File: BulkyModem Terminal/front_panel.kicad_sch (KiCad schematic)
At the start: 24 parts, among them J3 Module_Panel, U5 74HCT04

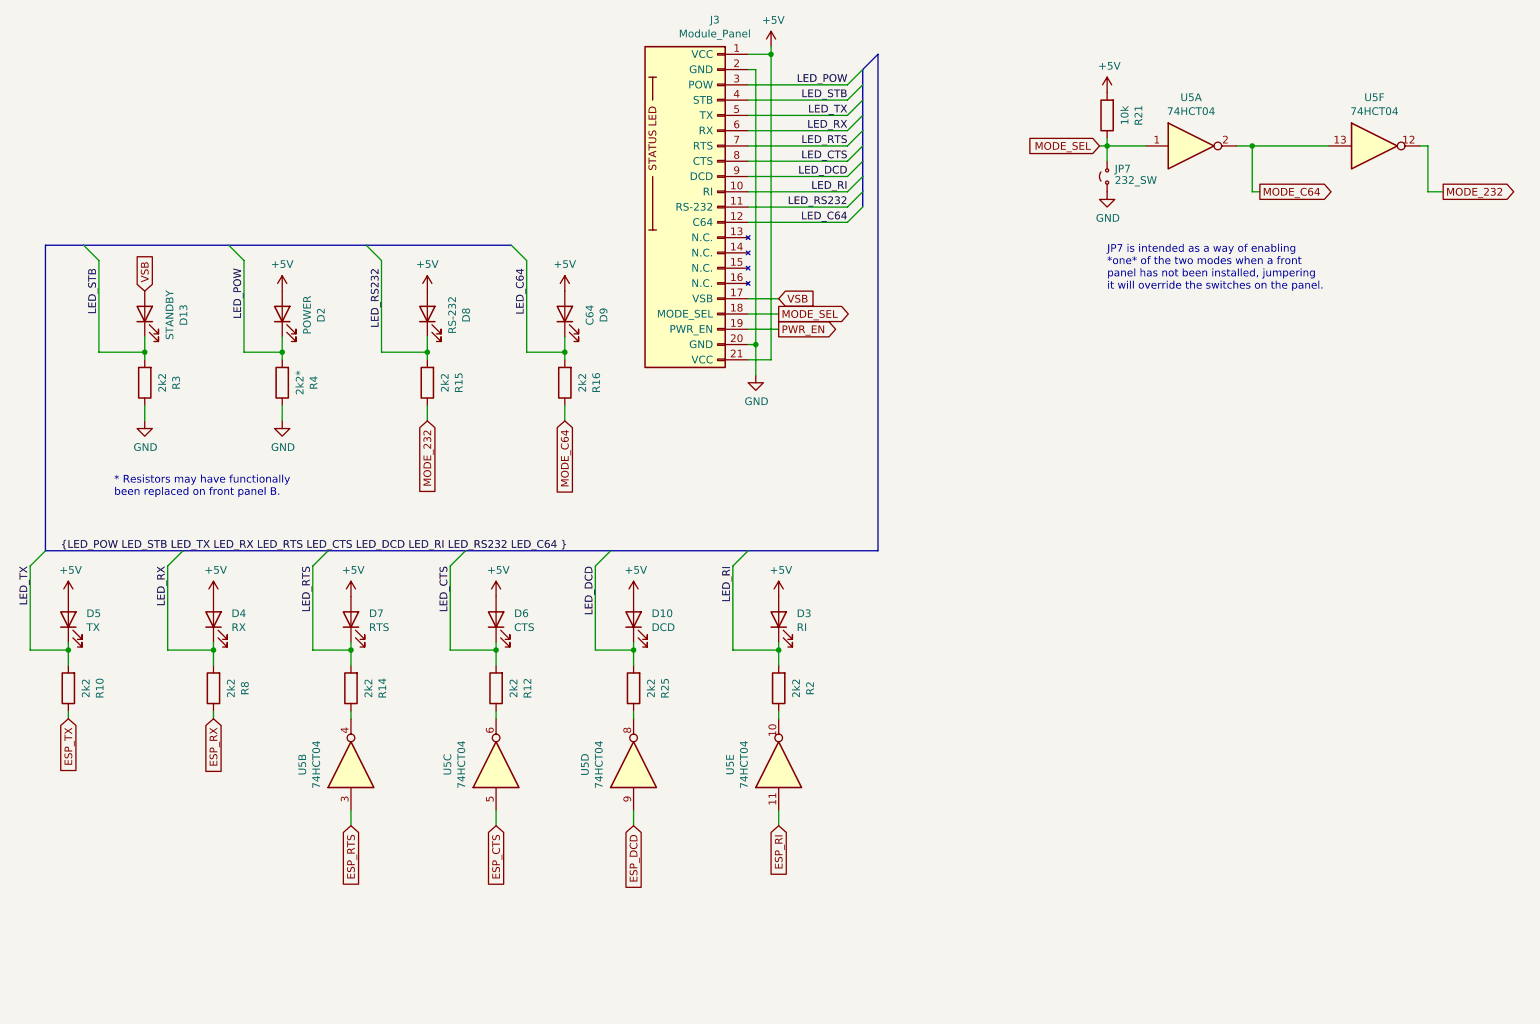
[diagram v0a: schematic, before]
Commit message: Terminal schematic (first draft)
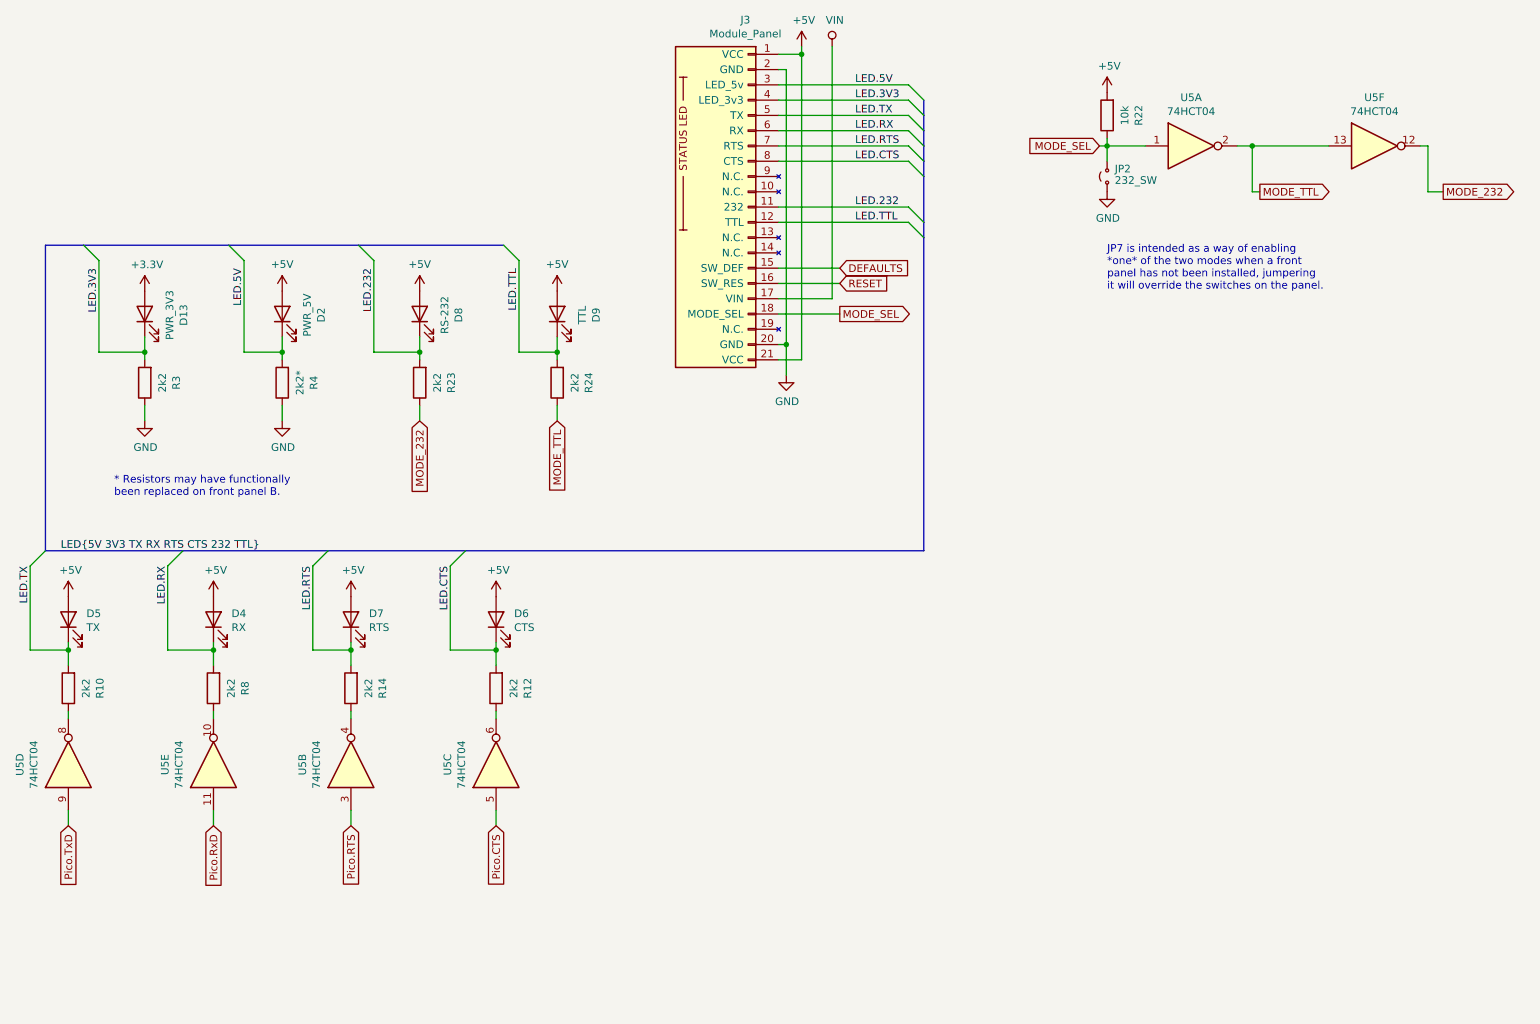
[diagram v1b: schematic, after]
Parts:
- removed D10: DCD, LED_THT:LED_D3.0mm, symbol Device:LED
- removed D3: RI, LED_THT:LED_D3.0mm, symbol Device:LED
- removed JP7: 232_SW, Connector_PinHeader_2.54mm:PinHeader_1x02_P2.54mm_Vertical, symbol Jumper:Jumper_2_Small_Open
- removed R15, R16, R2, R25: 2k2, resistor:R_Axial_DIN0207_L6.3mm_D2.5mm_P10.16mm_Horizontal, symbol Device:R
- removed R21: 10k, resistor:R_Axial_DIN0207_L6.3mm_D2.5mm_P10.16mm_Horizontal, symbol Device:R
- added JP2: 232_SW, Connector_PinHeader_2.54mm:PinHeader_1x02_P2.54mm_Vertical, symbol Jumper:Jumper_2_Small_Open
- added R22: 10k, resistor:R_Axial_DIN0207_L6.3mm_D2.5mm_P10.16mm_Horizontal, symbol Device:R
- added R23, R24: 2k2, resistor:R_Axial_DIN0207_L6.3mm_D2.5mm_P10.16mm_Horizontal, symbol Device:R
- D13: value STANDBY -> PWR_3V3
- D2: value POWER -> PWR_5V
- D9: value C64 -> TTL
- J3: symbol BulkyModem:Module_Panel -> BulkyModem:Terminal_Panel
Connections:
- net ESP_RX is gone; now on an unnamed net: R8.1
- net ESP_TX is gone; now on an unnamed net: R10.1
- net +5V: now also R22.2
- net GND: now also JP2.1 (A)
- net MODE_232: now also R23.1
- net MODE_SEL: now also JP2.2 (B), R22.1
- net DEFAULTS: now reaches J3.15 (SW_DEF)
- net RESET: now reaches J3.16 (SW_RES)
- net ESP_CTS renamed Pico.CTS
- net ESP_DCD renamed Pico.TxD
- net ESP_RI renamed Pico.RxD
- net ESP_RTS renamed Pico.RTS
- net LED_C64 renamed LED.TTL
- net LED.TTL: now also R24.2
- net LED_CTS renamed LED.CTS
- net LED_DCD: no longer names the net of J3.9 (N.C.)
- net LED_POW renamed LED.5V
- net LED_RI: no longer names the net of J3.10 (N.C.)
- net LED_RS232 renamed LED.232
- net LED.232: now also R23.2
- net LED_RTS renamed LED.RTS
- net LED_RX renamed LED.RX
- net LED_STB renamed LED.3V3
- net LED_TX renamed LED.TX
- net MODE_C64 renamed MODE_TTL
- net MODE_TTL: now also R24.1
- net PWR_EN: no longer names the net of J3.19 (N.C.)
- net VSB renamed +3.3V
- net +3.3V: no longer J3.17 (VSB)
- new net VIN: J3.17 (VIN)

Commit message: Part of a layout
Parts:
- removed D13: PWR_3V3, LED_THT:LED_D3.0mm, symbol Device:LED
- removed D2: PWR_5V, LED_THT:LED_D3.0mm, symbol Device:LED
- removed R3: 2k2, resistor:R_Axial_DIN0207_L6.3mm_D2.5mm_P10.16mm_Horizontal, symbol Device:R
- J3: footprint BulkyModem:Module_Panel -> BulkyModem:Terminal_Panel
- R4: value 2k2* -> 2k2
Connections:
- net LED.232: now also J3.9 (EN_232); no longer J3.11 (232)
- net LED.TTL: now also J3.10 (EN_TTL); no longer J3.12 (TTL)
- net LED.3V3: no longer names the net of J3.4 (N.C.)
- net LED.5V renamed LED.POW
- no-connect marks 0 -> 5
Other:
- note removed: "* Resistors may have functionally been replaced on front panel B."
- moved on the sheet: R4

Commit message: Added remaining tracks
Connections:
- no-connect marks 5 -> 6
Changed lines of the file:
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@@
+	)
+	(no_connect
+		(at 158.75 74.93)
 	)
 	(no_connect
@@
 		)
 	)
-	(label "LED{5V 3V3 TX RX RTS CTS 232 TTL}"
+	(label "LED{POW TX RX RTS CTS 232 TTL}"
 		(at 39.37 111.76 0)
 		(fields_autoplaced yes)

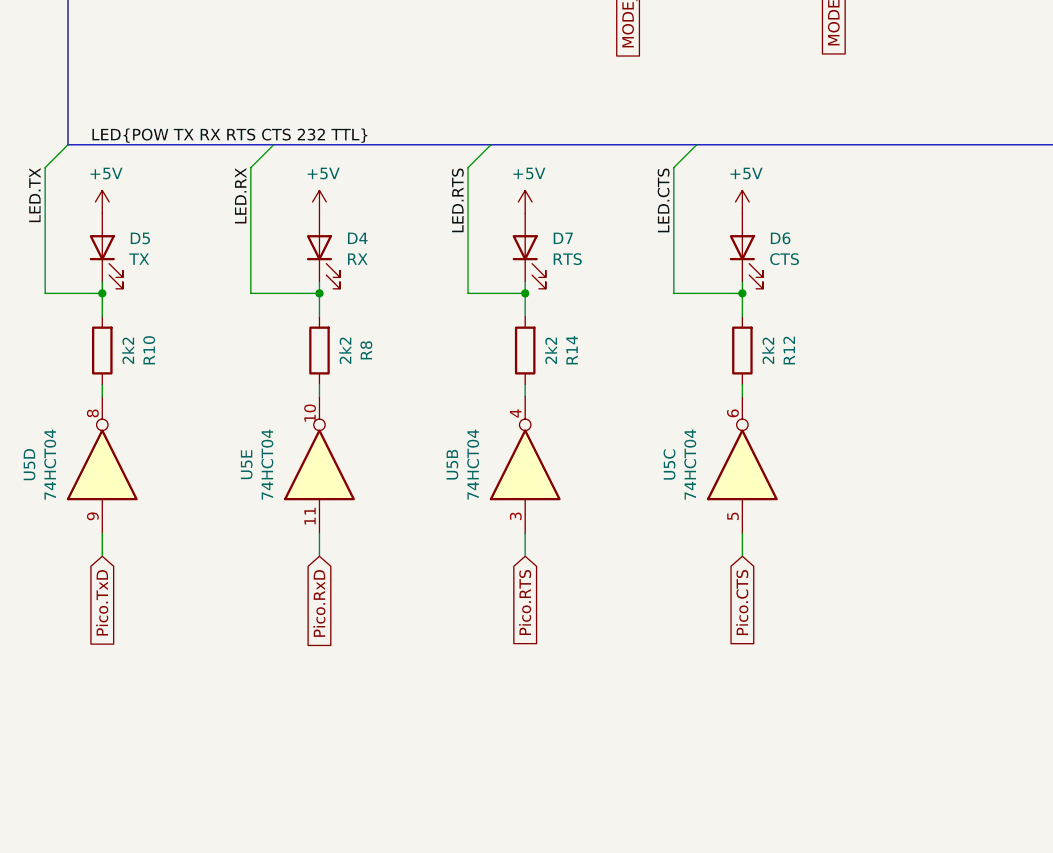
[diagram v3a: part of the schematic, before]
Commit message: Flipped serial LEDs
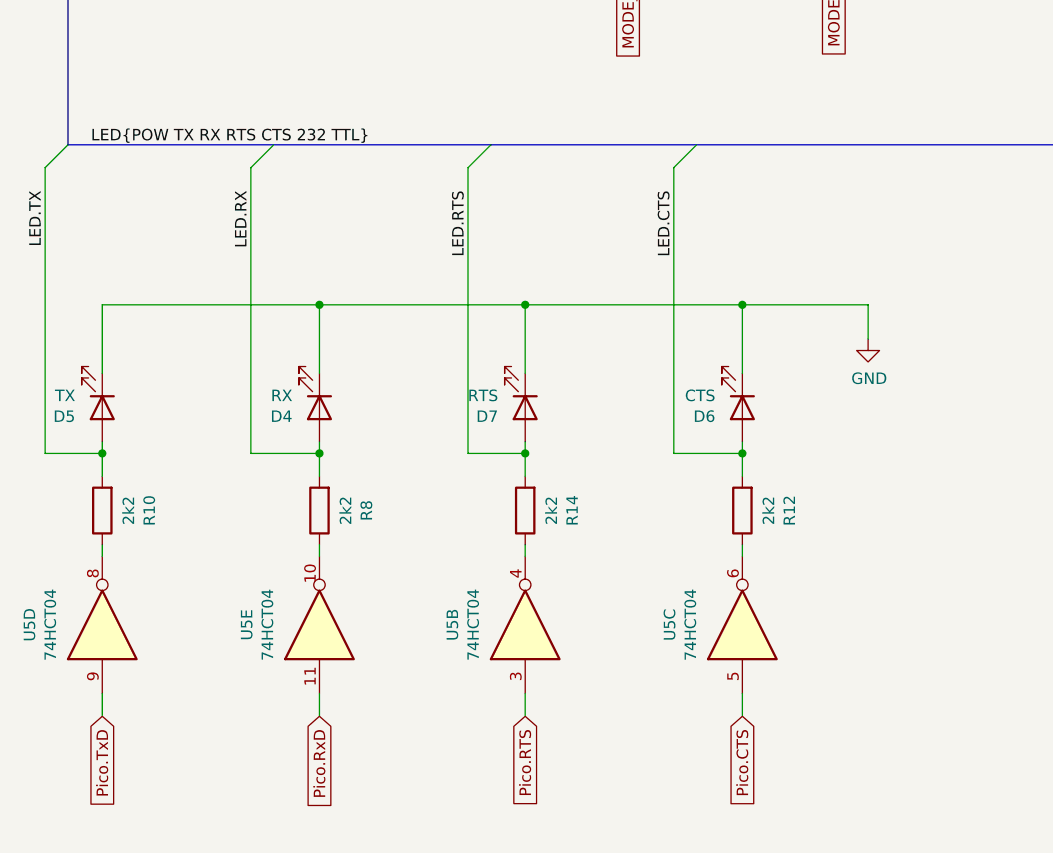
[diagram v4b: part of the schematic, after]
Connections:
- net +5V: no longer D4.2 (A), D5.2 (A), D6.2 (A), D7.2 (A)
- net GND: now also D4.1 (K), D5.1 (K), D6.1 (K), D7.1 (K)
- net LED.CTS: now also D6.2 (A); no longer D6.1 (K)
- net LED.RTS: now also D7.2 (A); no longer D7.1 (K)
- net LED.RX: now also D4.2 (A); no longer D4.1 (K)
- net LED.TX: now also D5.2 (A); no longer D5.1 (K)
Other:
- moved on the sheet: D4, D5, D6, D7, R10, R12, R14, R8, U5B, U5C, U5D, U5E
